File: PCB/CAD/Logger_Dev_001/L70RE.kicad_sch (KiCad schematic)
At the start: 2 parts, among them J3 CONSMA002-SMD-G-T, U5 L70-R

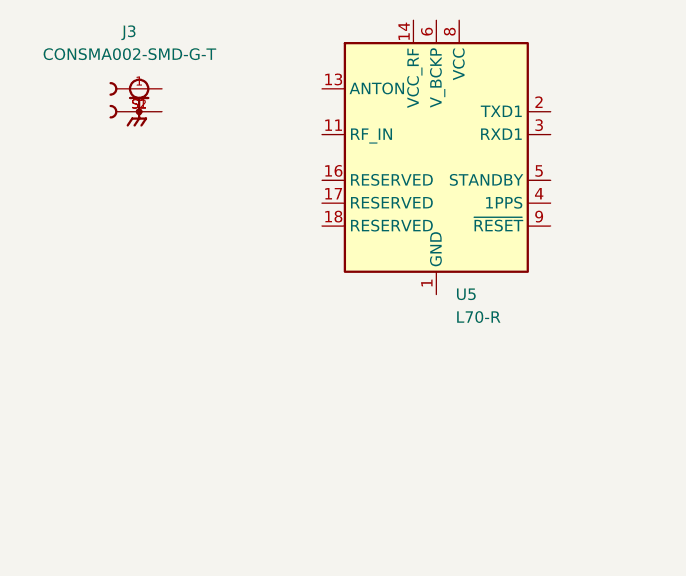
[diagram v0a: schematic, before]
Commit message: JLCPCB Component Updates
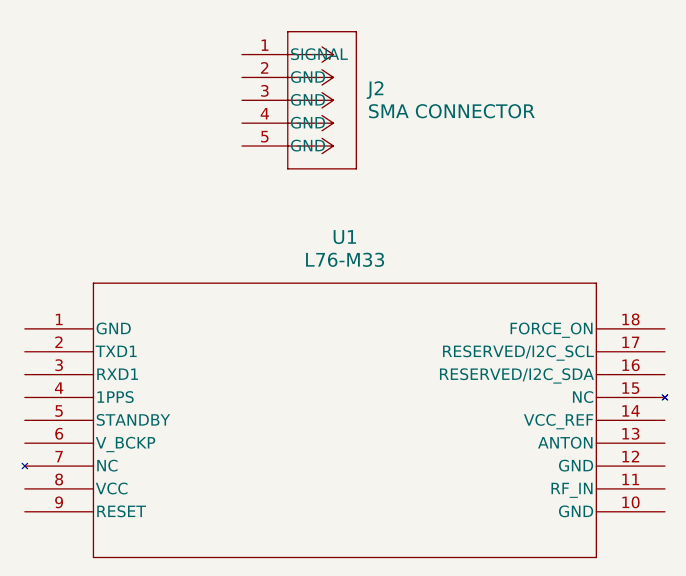
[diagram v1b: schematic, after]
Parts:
- removed J3: CONSMA002-SMD-G-T, CONSMA002-SMD-G-T:LINX_CONSMA002-SMD-G-T, symbol CONSMA002-SMD-G-T:CONSMA002-SMD-G-T
- removed U5: L70-R, RF_GPS:Quectel_L70-R, symbol RF_GPS:L70-R
- added J2: SMA CONNECTOR, CONN_SMA CONNECTOR_LPR, symbol 2025-10-24_05-52-57:SMA_CONNECTOR
- added U1: L76-M33, L76_QWS, symbol L76L-M33 GNSS:L76-M33
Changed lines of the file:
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@@
 	(paper "A4")
 	(symbol
-		(lib_id "RF_GPS:L70-R")
-		(at 162.56 86.36 0)
+		(lib_id "L76L-M33 GNSS:L76-M33")
+		(at 116.84 105.41 0)
 		(unit 1)
 		(exclude_from_sim no)
@@
 		(dnp no)
 		(fields_autoplaced yes)
-		(property "Reference" "U5"
-			(at 164.7033 101.6 0)
+		(property "Reference" "U1"
+			(at 152.4 95.25 0)
+			(effects
+				(font
+					(size 1.524 1.524)
+				)
+			)
+		)
+		(property "Value" "L76-M33"
+			(at 152.4 97.79 0)
+			(effects
+				(font
+					(size 1.524 1.524)
+				)
+			)
+		)
+		(property "Footprint" "L76_QWS"
+			(at 116.84 105.41 0)
 			(effects
 				(font
 					(size 1.27 1.27)
+					(italic yes)
 				)
-				(justify left)
+				(hide yes)
 			)
 		)
-		(property "Value" "L70-R"
-			(at 164.7033 104.14 0)
+		(property "Datasheet" "L76-M33"
+			(at 116.84 105.41 0)
 			(effects
 				(font
 					(size 1.27 1.27)
+					(italic yes)
 				)
-				(justify left)
+				(hide yes)
 			)
 		)
-		(property "Footprint" "RF_GPS:Quectel_L70-R"
-			(at 162.56 113.03 0)
+		(property "Description" ""
+			(at 116.84 105.41 0)
 			(effects
 				(font
@@
 			)
 		)
-		(property "Datasheet" "https://www.quectel.com/product/gps-only-l70-r"
-			(at 162.56 116.84 0)
+		(pin "16"
+		)
+		(pin "15"
+		)
+		(pin "5"
+		)
+		(pin "2"
+		)
+		(pin "3"
+		)
+		(pin "4"
+		)
+		(pin "6"
+		)
+		(pin "7"
+		)
+		(pin "8"
+		)
+		(pin "1"
+		)
+		(pin "9"
+		)
+		(pin "18"
+		)
+		(pin "17"
+		)
+		(pin "12"
+		)
+		(pin "13"
+		)
+		(pin "11"
+		)
+		(pin "10"
+		)
+		(pin "14"
+		)
+		(instances
+			(project ""
+				(path "/9546b831-c7ee-4f40-8993-5fd5a38d4078/b37dc544-49d2-4960-bf8e-49b471c058c3"
+					(reference "U1")
+					(unit 1)
+				)
+			)
+		)
+	)
+	(symbol
+		(lib_id "2025-10-24_05-52-57:SMA_CONNECTOR")
+		(at 140.97 74.93 0)
+		(unit 1)
+		(exclude_from_sim no)
+		(in_bom yes)
+		(on_board yes)
+		(dnp no)
+		(fields_autoplaced yes)
+		(property "Reference" "J2"
+			(at 154.94 78.7399 0)
+			(effects
+				(font
+					(size 1.524 1.524)
+				)
+				(justify left)
+			)
+		)
+		(property "Value" "SMA CONNECTOR"
+			(at 154.94 81.2799 0)
+			(effects
+				(font
+					(size 1.524 1.524)
+				)
+				(justify left)
+			)
+		)
+		(property "Footprint" "CONN_SMA CONNECTOR_LPR"
+			(at 140.97 74.93 0)
+			(effects
+				(font
+					(size 1.27 1.27)
+					(italic yes)
+				)
+				(hide yes)
+			)
+		)
+		(property "Datasheet" "SMA CONNECTOR"
+			(at 140.97 74.93 0)
+			(effects
+				(font
+					(size 1.27 1.27)
+					(italic yes)
+				)
+				(hide yes)
+			)
+		)
+		(property "Description" ""
+			(at 140.97 74.93 0)
 			(effects
 				(font
@@
 			)
 		)
-		(property "Description" "Quectel GPS Module"
-			(at 162.56 86.36 0)
-			(effects
-				(font
-					(size 1.27 1.27)
-				)
-				(hide yes)
-			)
+		(pin "5"
 		)
-		(pin "13"
-		)
-		(pin "15"
-		)
-		(pin "6"
-		)
-		(pin "10"
-		)
-		(pin "14"
-		)
-		(pin "11"
-		)
-		(pin "16"
-		)
-		(pin "17"
-		)
-		(pin "18"
+		(pin "2"
 		)
 		(pin "1"
 		)
-		(pin "7"
-		)
-		(pin "5"
-		)
-		(pin "8"
-		)
 		(pin "3"
-		)
-		(pin "9"
 		)
 		(pin "4"
 		)
-		(pin "12"
-		)
-		(pin "2"
-		)
 		(instances
-			(project "Logger_Dev_001"
+			(project ""
 				(path "/9546b831-c7ee-4f40-8993-5fd5a38d4078/b37dc544-49d2-4960-bf8e-49b471c058c3"
-					(reference "U5")
+					(reference "J2")
 					(unit 1)
 				)
-			)
-		)
-	)
-	(symbol
-		(lib_id "CONSMA002-SMD-G-T:CONSMA002-SMD-G-T")
-		(at 129.54 78.74 0)
-		(unit 1)
-		(exclude_from_sim no)
-		(in_bom yes)
-		(on_board yes)
-		(dnp no)
-		(fields_autoplaced yes)
-		(property "Reference" "J3"
-			(at 128.4605 72.39 0)
-			(effects
-				(font
-					(size 1.27 1.27)
-				)
-			)
-		)
-		(property "Value" "CONSMA002-SMD-G-T"
-			(at 128.4605 74.93 0)
-			(effects
-				(font
-					(size 1.27 1.27)
-				)
-			)
-		)
-		(property "Footprint" "CONSMA002-SMD-G-T:LINX_CONSMA002-SMD-G-T"
-			(at 129.54 78.74 0)
-			(effects
-				(font
-					(size 1.27 1.27)
-				)
-				(justify bottom)
-				(hide yes)
-			)
-		)
-		(property "Datasheet" ""
-			(at 129.54 78.74 0)
-			(effects
-				(font
-					(size 1.27 1.27)
-				)
-				(hide yes)
-			)
-		)
-		(property "Description" ""
-			(at 129.54 78.74 0)
-			(effects
-				(font
-					(size 1.27 1.27)
-				)
-				(hide yes)
-			)
-		)
-		(property "SnapEDA_Link" "https://www.snapeda.com/parts/CONSMA002-SMD-G-T/Linx/view-part/?ref=snap"
-			(at 129.54 78.74 0)
-			(effects
-				(font
-					(size 1.27 1.27)
-				)
-				(justify bottom)
-				(hide yes)
-			)
-		)
-		(property "Check_prices" "https://www.snapeda.com/parts/CONSMA002-SMD-G-T/Linx/view-part/?ref=eda"
-			(at 129.54 78.74 0)
-			(effects
-				(font
-					(size 1.27 1.27)
-				)
-				(justify bottom)
-				(hide yes)
-			)
-		)
-		(property "Package" "None"
-			(at 129.54 78.74 0)
-			(effects
-				(font
-					(size 1.27 1.27)
-				)
-				(justify bottom)
-				(hide yes)
-			)
-		)
-		(property "Price" "None"
-			(at 129.54 78.74 0)
-			(effects
-				(font
-					(size 1.27 1.27)
-				)
-				(justify bottom)
-				(hide yes)
-			)
-		)
-		(property "MF" "Linx Technologies"
-			(at 129.54 78.74 0)
-			(effects
-				(font
-					(size 1.27 1.27)
-				)
-				(justify bottom)
-				(hide yes)
-			)
-		)
-		(property "MP" "CONSMA002-SMD-G-T"
-			(at 129.54 78.74 0)
-			(effects
-				(font
-					(size 1.27 1.27)
-				)
-				(justify bottom)
-				(hide yes)
-			)
-		)
-		(property "Purchase-URL" "https://www.snapeda.com/api/url_track_click_mouser/?unipart_id=4479740&manufacturer=Linx Technologies&part_name=CONSMA002-SMD-G-T&search_term=None"
-			(at 129.54 78.74 0)
-			(effects
-				(font
-					(size 1.27 1.27)
-				)
-				(justify bottom)
-				(hide yes)
-			)
-		)
-		(property "Availability" "In Stock"
-			(at 129.54 78.74 0)
-			(effects
-				(font
-					(size 1.27 1.27)
-				)
-				(justify bottom)
-				(hide yes)
-			)
-		)
-		(property "Description_1" "SMA Jack 50 Ohm PCB Surface Mount"
-			(at 129.54 78.74 0)
-			(effects
-				(font
-					(size 1.27 1.27)
-				)
-				(justify bottom)
-				(hide yes)
-			)
-		)
-		(pin "S2"
-		)
-		(pin "S1"
-		)
-		(pin "1"
-		)
-		(instances
-			(project "Logger_Dev_001"
-				(path "/9546b831-c7ee-4f40-8993-5fd5a38d4078/b37dc544-49d2-4960-bf8e-49b471c058c3"
-					(reference "J3")
-					(unit 1)
-				)

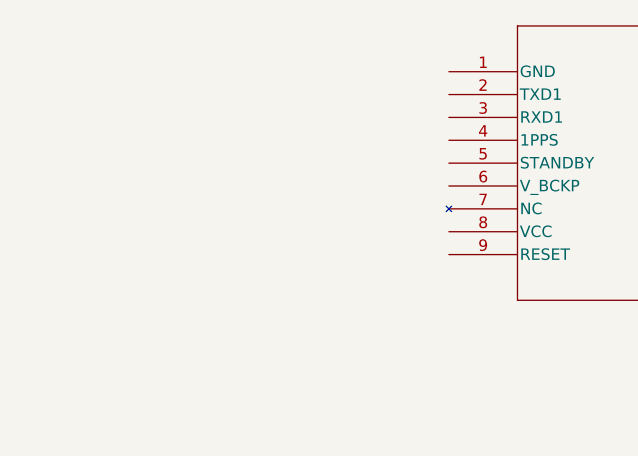
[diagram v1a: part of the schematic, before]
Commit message: Power input Schematic
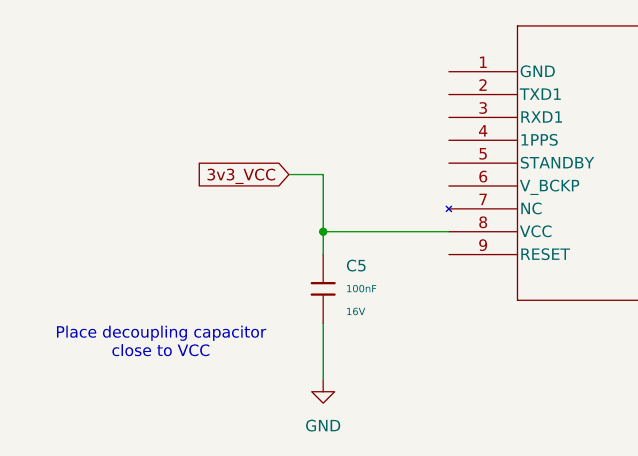
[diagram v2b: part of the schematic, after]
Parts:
- added C5: 100nF, PCM_JLCPCB:C_0402, symbol PCM_JLCPCB-Capacitors:0402,100nF
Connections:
- net 3v3_VCC: now reaches U1.8 (VCC)
- net 3v3_VCC: now also C5.1
- new net GND: C5.2
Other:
- note added: "Place decoupling capacitor close to VCC"

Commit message: Updated Schematic
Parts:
- added TP13: GPS_TX_TP, symbol Connector:TestPoint
- added TP14: GPS_RX_TP, symbol Connector:TestPoint
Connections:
- net !GPS_TX: now reaches U1.2 (TXD1)
- net !GPS_TX: now also TP13.1
- net !GPS_RX: now reaches U1.3 (RXD1)
- net !GPS_RX: now also TP14.1
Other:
- company: (none) -> Jake Odgers
- title: (none) -> Mileage Logger

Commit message: Updated Schematic
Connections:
- net GND: now also J2.2 (GND), J2.3 (GND), J2.4 (GND), J2.5 (GND), U1.10 (GND), U1.12 (GND)
- net at U1.11 (RF_IN): now also J2.1 (SIGNAL)
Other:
- moved on the sheet: C5, J2, U1

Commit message: Schematic finalised
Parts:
- added BT1: CR2032-BS-6-1, CR2032-BS-6-1:BAT_CR2032-BS-6-1, symbol CR2032-BS-6-1:CR2032-BS-6-1
- added C14, C15: 100nF, PCM_JLCPCB:C_0402, symbol PCM_JLCPCB-Capacitors:0402,100nF
- added D5: SS14, PCM_JLCPCB:D_SMA, symbol PCM_JLCPCB-Diodes:Schottky,SS14
- added D6: Red, PCM_JLCPCB:D_0805, symbol PCM_JLCPCB-Diodes:LED,0805,Red
- added L1: 47nH_600mA, PCM_JLCPCB:L_0603, symbol PCM_JLCPCB-Inductors:47nH_600mA
- added Q2: MMBT3904, PCM_JLCPCB:Q_SOT-23, symbol PCM_JLCPCB-Transistors:NPN,MMBT3904
- added R17: 10kΩ, PCM_JLCPCB:R_0402, symbol PCM_JLCPCB-Resistors:0402,10kΩ
- added R18, R19: 10Ω, PCM_JLCPCB:R_0402, symbol PCM_JLCPCB-Resistors:0402,10Ω
- added R20: 220Ω, PCM_JLCPCB:R_0402, symbol PCM_JLCPCB-Resistors:0402,220Ω
- added R21: 5.1kΩ, PCM_JLCPCB:R_0402, symbol PCM_JLCPCB-Resistors:0402,5.1kΩ
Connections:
- net 3v3_VCC: now also R17.1, R20.1
- net GND: now also U1.1 (GND), BT1.N, C14.2, C15.2, Q2.2 (E)
- net at J2.1 (SIGNAL), U1.11 (RF_IN): now also L1.2
- net at U1.14 (VCC_REF): now also C14.1, R18.1
- net 1PPS: now reaches U1.4 (1PPS)
- net 1PPS: now also R21.1
- net VBAT_2032: now reaches U1.6 (V_BCKP)
- net VBAT_2032: now also C15.1, R19.2
- net at U1.9 (RESET): now also R17.2
- new net: D5.1, R19.1
- new net: BT1.P, D5.2
- new net: D6.2, R20.2
- new net: D6.1, Q2.3 (C)
- new net: L1.1, R18.2
- new net: Q2.1 (B), R21.2
- no-connect marks 0 -> 5
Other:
- note added: "2.5 Years at 10uA"
- note added: "Place Bypass Capacitor close to VCC_REF"
- moved on the sheet: C5, J2, TP13, TP14, U1

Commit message: Update some footprints
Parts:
- BT1: footprint CR2032-BS-6-1:BAT_CR2032-BS-6-1 -> CR2032:BAT_CR2032-BS-6-1
- J2: footprint CONN_SMA CONNECTOR_LPR -> (none)
- U1: footprint L76_QWS -> GPS L76-M33:L76_QWS
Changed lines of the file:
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@@
 			)
 		)
-		(property "Footprint" "L76_QWS"
+		(property "Footprint" "GPS L76-M33:L76_QWS"
 			(at 87.63 101.6 0)
 			(effects
@@
 			)
 		)
-		(property "Footprint" "CONN_SMA CONNECTOR_LPR"
+		(property "Footprint" ""
 			(at 194.31 119.38 0)
 			(effects
@@
 			)
 		)
-		(property "Footprint" "CR2032-BS-6-1:BAT_CR2032-BS-6-1"
+		(property "Footprint" "CR2032:BAT_CR2032-BS-6-1"
 			(at 44.45 46.99 0)
 			(effects

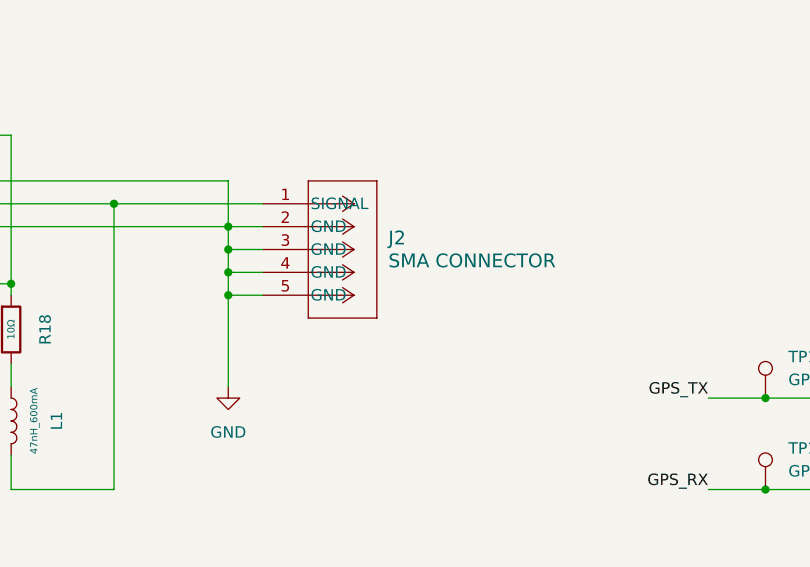
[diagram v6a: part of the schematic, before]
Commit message: Schematic Update for footprints
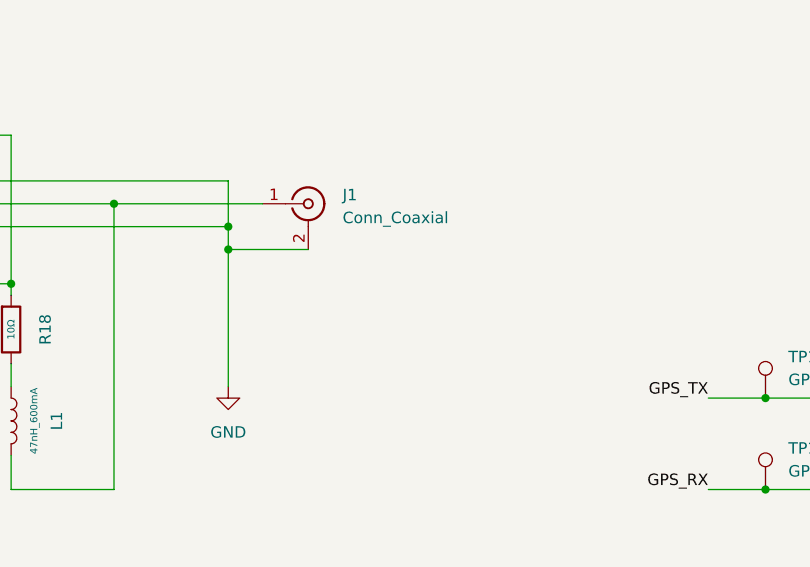
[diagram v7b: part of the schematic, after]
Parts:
- removed J2: SMA CONNECTOR, symbol 2025-10-24_05-52-57:SMA_CONNECTOR
- added J1: Conn_Coaxial, LPRS_SMA_CONNECTOR:LPRS_SMA_CONNECTOR, symbol Connector:Conn_Coaxial
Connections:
- net GND: now also J1.2 (Ext)
- net at L1.2, U1.11 (RF_IN): now also J1.1 (In)
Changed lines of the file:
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@@
-	)
-	(junction
-		(at 190.5 127)
-		(diameter 0)
-		(color 0 0 0 0)
 	)
 	(junction
@@
 		(color 0 0 0 0)
 	)
-	(junction
-		(at 190.5 129.54)
-		(diameter 0)
-		(color 0 0 0 0)
-	)
 	(no_connect
 		(at 161.29 106.68)
@@
 	(wire
 		(pts
-			(xy 190.5 129.54) (xy 190.5 139.7)
-		)
-		(stroke
-			(width 0)
-			(type default)
-		)
-	)
-	(wire
-		(pts
 			(xy 73.66 36.83) (xy 77.47 36.83)
 		)
@@
 	(wire
 		(pts
-			(xy 194.31 129.54) (xy 190.5 129.54)
-		)
-		(stroke
-			(width 0)
-			(type default)
-		)
-	)
-	(wire
-		(pts
 			(xy 190.5 116.84) (xy 190.5 121.92)
 		)
@@
 	(wire
 		(pts
-			(xy 190.5 129.54) (xy 190.5 127)
-		)
-		(stroke
-			(width 0)
-			(type default)
-		)
-	)
-	(wire
-		(pts
 			(xy 166.37 151.13) (xy 177.8 151.13)
 		)
@@
 	(wire
 		(pts
-			(xy 190.5 124.46) (xy 190.5 127)
-		)
-		(stroke
-			(width 0)
-			(type default)
-		)
-	)
-	(wire
-		(pts
 			(xy 82.55 133.35) (xy 82.55 139.7)
 		)
@@
 	(wire
 		(pts
+			(xy 190.5 124.46) (xy 190.5 139.7)
+		)
+		(stroke
+			(width 0)
+			(type default)
+		)
+	)
+	(wire
+		(pts
 			(xy 63.5 110.49) (xy 57.15 110.49)
 		)
@@
 	(wire
 		(pts
-			(xy 194.31 124.46) (xy 190.5 124.46)
-		)
-		(stroke
-			(width 0)
-			(type default)
-		)
-	)
-	(wire
-		(pts
 			(xy 72.39 121.92) (xy 72.39 129.54)
 		)
@@
 	(wire
 		(pts
+			(xy 190.5 124.46) (xy 199.39 124.46)
+		)
+		(stroke
+			(width 0)
+			(type default)
+		)
+	)
+	(wire
+		(pts
 			(xy 44.45 54.61) (xy 44.45 57.15)
 		)
@@
 	(wire
 		(pts
-			(xy 194.31 127) (xy 190.5 127)
-		)
-		(stroke
-			(width 0)
-			(type default)
-		)
-	)
-	(wire
-		(pts
 			(xy 158.75 104.14) (xy 161.29 104.14)
 		)
@@
 		(pts
 			(xy 243.84 140.97) (xy 250.19 140.97)
-		)
-		(stroke
-			(width 0)
-			(type default)
-		)
-	)
-	(wire
-		(pts
-			(xy 190.5 121.92) (xy 194.31 121.92)
 		)
 		(stroke
@@
 	)
 	(symbol
-		(lib_id "2025-10-24_05-52-57:SMA_CONNECTOR")
-		(at 194.31 119.38 0)
+		(lib_id "Connector:Conn_Coaxial")
+		(at 199.39 119.38 0)
 		(unit 1)
 		(exclude_from_sim no)
@@
 		(dnp no)
 		(fields_autoplaced yes)
-		(property "Reference" "J2"
-			(at 208.28 123.1899 0)
-			(effects
-				(font
-					(size 1.524 1.524)
+		(property "Reference" "J1"
+			(at 203.2 118.4031 0)
+			(effects
+				(font
+					(size 1.27 1.27)
 				)
 				(justify left)
 			)
 		)
-		(property "Value" "SMA CONNECTOR"
-			(at 208.28 125.7299 0)
-			(effects
-				(font
-					(size 1.524 1.524)
+		(property "Value" "Conn_Coaxial"
+			(at 203.2 120.9431 0)
+			(effects
+				(font
+					(size 1.27 1.27)
 				)
 				(justify left)
 			)
 		)
-		(property "Footprint" ""
-			(at 194.31 119.38 0)
-			(effects
-				(font
-					(size 1.27 1.27)
-					(italic yes)
-				)
-				(hide yes)
-			)
-		)
-		(property "Datasheet" "SMA CONNECTOR"
-			(at 194.31 119.38 0)
-			(effects
-				(font
-					(size 1.27 1.27)
-					(italic yes)
-				)
-				(hide yes)
-			)
-		)
-		(property "Description" ""
-			(at 194.31 119.38 0)
-			(effects
-				(font
-					(size 1.27 1.27)
-				)
-				(hide yes)
-			)
-		)
-		(pin "5"
+		(property "Footprint" "LPRS_SMA_CONNECTOR:LPRS_SMA_CONNECTOR"
+			(at 199.39 119.38 0)
+			(effects
+				(font
+					(size 1.27 1.27)
+				)
+				(hide yes)
+			)
+		)
+		(property "Datasheet" "~"
+			(at 199.39 119.38 0)
+			(effects
+				(font
+					(size 1.27 1.27)
+				)
+				(hide yes)
+			)
+		)
+		(property "Description" "coaxial connector (BNC, SMA, SMB, SMC, Cinch/RCA, LEMO, ...)"
+			(at 199.39 119.38 0)
+			(effects
+				(font
+					(size 1.27 1.27)
+				)
+				(hide yes)
+			)
 		)
 		(pin "2"
 		)
 		(pin "1"
-		)
-		(pin "3"
-		)
-		(pin "4"
 		)
 		(instances
 			(project ""
 				(path "/9546b831-c7ee-4f40-8993-5fd5a38d4078/b37dc544-49d2-4960-bf8e-49b471c058c3"
-					(reference "J2")
+					(reference "J1")
 					(unit 1)
 				)

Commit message: Schematic Finished
Still need to check BOM
Starting to layout PCB
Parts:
- J1: footprint LPRS_SMA_CONNECTOR:LPRS_SMA_CONNECTOR -> Connector_Coaxial:SMA_Amphenol_901-143_Horizontal
- TP13, TP14: footprint (none) -> TestPoint:TestPoint_Pad_D2.5mm
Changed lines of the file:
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@@
 			)
 		)
-		(property "Footprint" "LPRS_SMA_CONNECTOR:LPRS_SMA_CONNECTOR"
+		(property "Footprint" "Connector_Coaxial:SMA_Amphenol_901-143_Horizontal"
 			(at 199.39 119.38 0)
 			(effects
@@
 			)
 		)
-		(property "Footprint" ""
+		(property "Footprint" "TestPoint:TestPoint_Pad_D2.5mm"
 			(at 255.27 151.13 0)
 			(effects
@@
 			)
 		)
-		(property "Footprint" ""
+		(property "Footprint" "TestPoint:TestPoint_Pad_D2.5mm"
 			(at 255.27 140.97 0)
 			(effects
